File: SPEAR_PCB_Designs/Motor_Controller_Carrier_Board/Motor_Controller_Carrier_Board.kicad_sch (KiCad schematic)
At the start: 16 parts, among them J1 Conn_01x02_Pin, J2 Conn_01x02_Pin, J3 Conn_01x02_Pin, J4 JST_S4B-XH-A-1, U1 AP63203WU

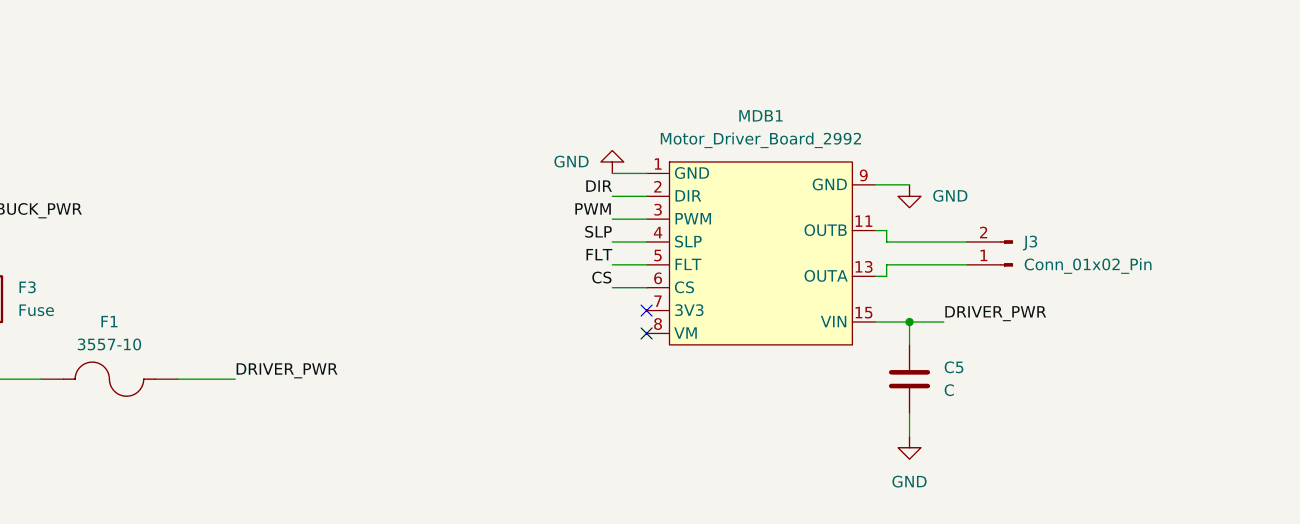
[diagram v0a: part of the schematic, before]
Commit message: Moved power traces to the front and made minor adjustments to the layout of the carrier board
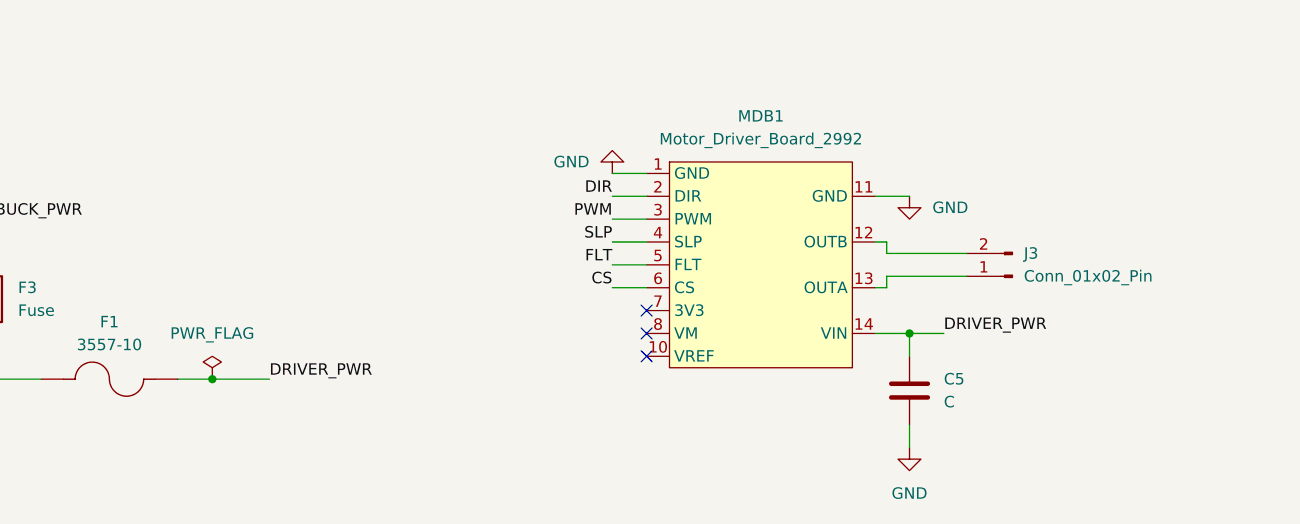
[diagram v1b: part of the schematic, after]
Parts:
- C1: DigiKey_Part_Number (none) -> 445-173297-1-ND
- C2, C4: DigiKey_Part_Number (none) -> 445-173319-1-ND
- C3: DigiKey_Part_Number (none) -> 56-K104K15X7RF53H5G-ND
- C5: DigiKey_Part_Number (none) -> 493-15942-ND
- F1: DigiKey_Part_Number (none) -> 36-3557-10-ND
- F2: DigiKey_Part_Number (none) -> 36-3557-15-ND
- F3: DigiKey_Part_Number (none) -> F5502CT-ND
- J4: DigiKey_Part_Number (none) -> 455-S4B-XH-A-1-ND
- L1: DigiKey_Part_Number (none) -> 732-74437368039CT-ND
- MCB1, MDB1: now left out of the parts list
- U1: DigiKey_Part_Number (none) -> AP63203WU-7DICT-ND
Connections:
- net DRIVER_PWR: now also MDB1.14 (VIN); no longer MDB1.15 (VIN), MDB1.16 (VIN)
- net GND: now also MDB1.11 (GND), MDB1.15 (GND), MDB1.16 (GND); no longer MDB1.10 (GND)
- net at J3.1 (Pin_1), MDB1.13 (OUTA): no longer MDB1.14 (OUTA)
- net at J3.2 (Pin_2), MDB1.12 (OUTB): no longer MDB1.11 (OUTB)
- no-connect marks 31 -> 32
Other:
- moved on the sheet: C5, J3

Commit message: Almost finished getting carrier board ready for fabrication
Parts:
- C3: footprint Capacitor_THT:C_Disc_D5.0mm_W2.5mm_P5.00mm -> Motor_Controller_Carrier_Board:C_Disc_D5.0mm_W2.5mm_P5.00mm
- J1, J2, J3: footprint Connector_AMASS:AMASS_XT30PW-M_1x02_P2.50mm_Horizontal -> SPEAR_Connectors:AMASS_XT30PW-M_1x02_P2.50mm_Horizontal_1; now left out of the parts list
- J4: footprint Connector_JST:JST_XH_S4B-XH-A-1_1x04_P2.50mm_Horizontal -> SPEAR_Connectors:JST_XH_S4B-XH-A-1_1x04_P2.50mm_Horizontal
- U1: footprint Package_TO_SOT_SMD:TSOT-23-6 -> Motor_Controller_Carrier_Board:TSOT-23-6
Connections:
- net DRIVER_PWR: now also MDB1.22 (VIN), MDB1.23 (VIN), MDB1.24 (VIN); no longer MDB1.14 (VIN)
- net GND: now also MDB1.12 (GND), MDB1.13 (GND), MDB1.14 (GND); no longer MDB1.16 (GND)
- net at J3.1 (Pin_1): now also MDB1.19 (OUTA), MDB1.20 (OUTA), MDB1.21 (OUTA); no longer MDB1.13 (OUTA)
- net at J3.2 (Pin_2): now also MDB1.16 (OUTB), MDB1.17 (OUTB), MDB1.18 (OUTB); no longer MDB1.12 (OUTB)
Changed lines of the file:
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@@
 		(unit 1)
 		(exclude_from_sim no)
-		(in_bom yes)
+		(in_bom no)
 		(on_board yes)
 		(dnp no)
@@
 			)
 		)
-		(property "Footprint" "Connector_AMASS:AMASS_XT30PW-M_1x02_P2.50mm_Horizontal"
+		(property "Footprint" "SPEAR_Connectors:AMASS_XT30PW-M_1x02_P2.50mm_Horizontal_1"
 			(at 213.36 130.81 0)
 			(effects
@@
 		(pin "16"
 		)
+		(pin "17"
+		)
+		(pin "19"
+		)
+		(pin "22"
+		)
+		(pin "24"
+		)
+		(pin "21"
+		)
+		(pin "18"
+		)
+		(pin "20"
+		)
+		(pin "23"
+		)
 		(instances
 			(project ""
@@
 			)
 		)
-		(property "Footprint" "Package_TO_SOT_SMD:TSOT-23-6"
+		(property "Footprint" "Motor_Controller_Carrier_Board:TSOT-23-6"
 			(at 64.77 96.52 0)
 			(effects
@@
 		(unit 1)
 		(exclude_from_sim no)
-		(in_bom yes)
+		(in_bom no)
 		(on_board yes)
 		(dnp no)
@@
 			)
 		)
-		(property "Footprint" "Connector_AMASS:AMASS_XT30PW-M_1x02_P2.50mm_Horizontal"
+		(property "Footprint" "SPEAR_Connectors:AMASS_XT30PW-M_1x02_P2.50mm_Horizontal_1"
 			(at 77.47 144.78 0)
 			(effects
@@
 			)
 		)
-		(property "Footprint" "Capacitor_THT:C_Disc_D5.0mm_W2.5mm_P5.00mm"
+		(property "Footprint" "Motor_Controller_Carrier_Board:C_Disc_D5.0mm_W2.5mm_P5.00mm"
 			(at 80.9752 73.66 0)
 			(effects
@@
 		(unit 1)
 		(exclude_from_sim no)
-		(in_bom yes)
+		(in_bom no)
 		(on_board yes)
 		(dnp no)
@@
 			)
 		)
-		(property "Footprint" "Connector_AMASS:AMASS_XT30PW-M_1x02_P2.50mm_Horizontal"
+		(property "Footprint" "SPEAR_Connectors:AMASS_XT30PW-M_1x02_P2.50mm_Horizontal_1"
 			(at 77.47 116.84 0)
 			(effects
@@
 			)
 		)
-		(property "Footprint" "Connector_JST:JST_XH_S4B-XH-A-1_1x04_P2.50mm_Horizontal"
+		(property "Footprint" "SPEAR_Connectors:JST_XH_S4B-XH-A-1_1x04_P2.50mm_Horizontal"
 			(at 238.76 74.93 0)
 			(effects

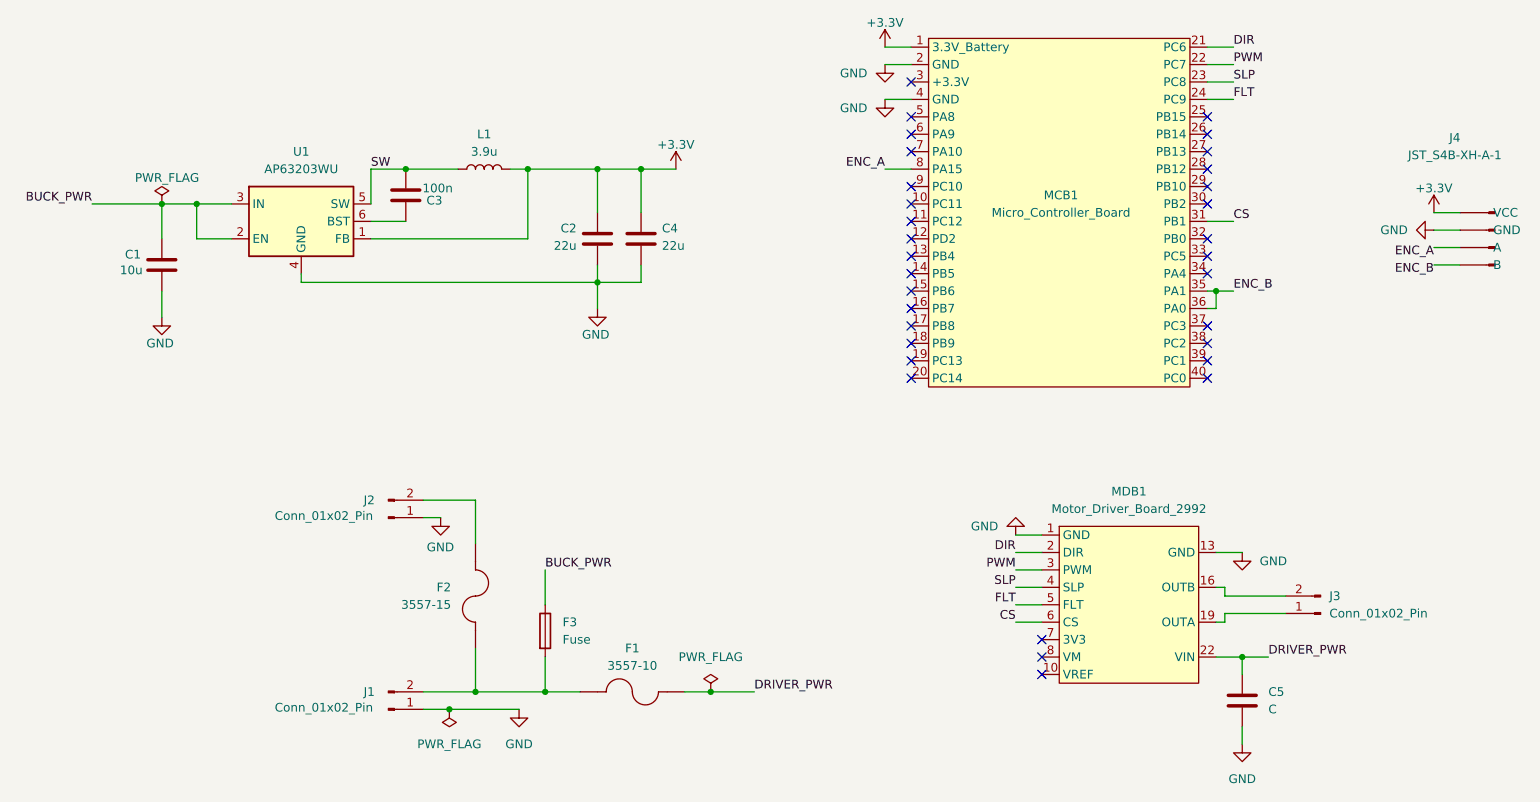
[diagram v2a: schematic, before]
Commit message: Added board-to-board connectors to schematic and swapped out THT capacitors for SMT ones in carrier board
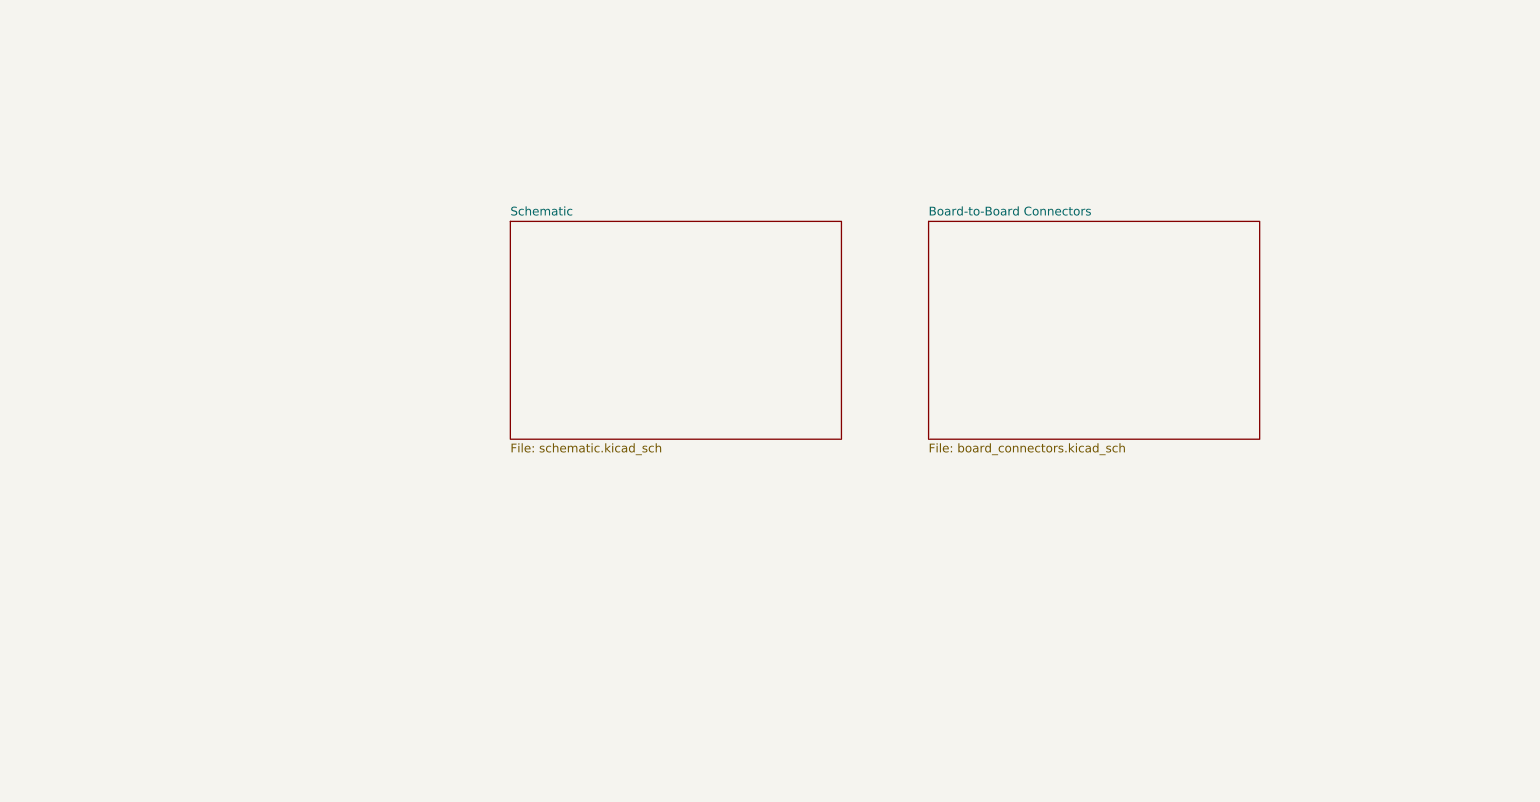
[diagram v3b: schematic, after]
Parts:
- removed C1: 10u, SPEAR_AP63203BuckConverter:CAP_FG20_TDK_C1, symbol Device:C
- removed C2, C4: 22u, SPEAR_AP63203BuckConverter:CAP_FG22_TDK_C2_C4, symbol Device:C
- removed C3: 100n, Motor_Controller_Carrier_Board:C_Disc_D5.0mm_W2.5mm_P5.00mm, symbol Device:C
- removed C5: C, Motor_Controller_Carrier_Board:CAP_UBY_18X20_NCH, symbol Device:C
- removed F1: 3557-10, Motor_Controller_Carrier_Board:FUSE_3557-10, symbol Motor_Controller_Carrier_Board:3557-10
- removed F2: 3557-15, Motor_Controller_Carrier_Board:FUSE_3557-15, symbol Motor_Controller_Carrier_Board:3557-10
- removed F3: Fuse, Motor_Controller_Carrier_Board:FUS_LITTELFUSE_392_LTF, symbol Device:Fuse
- removed J1, J2, J3: Conn_01x02_Pin, SPEAR_Connectors:AMASS_XT30PW-M_1x02_P2.50mm_Horizontal_1, symbol Connector:Conn_01x02_Pin
- removed J4: JST_S4B-XH-A-1, SPEAR_Connectors:JST_XH_S4B-XH-A-1_1x04_P2.50mm_Horizontal, symbol Motor_Controller_Carrier_Board:JST_S4B-XH-A-1
- removed L1: 3.9u, SPEAR_AP63203BuckConverter:L_Wurth_WE-LHMI-1040_L1, symbol Device:L
- removed MCB1: Micro_Controller_Board, SPEAR_Boards:Micro_Controller_Board, symbol SPEAR_Boards:Micro_Controller_Board
- removed MDB1: Motor_Driver_Board_2992, SPEAR_Boards:Motor_Driver_Board_2992, symbol SPEAR_Boards:Motor_Driver_Board_2992
- removed U1: AP63203WU, Motor_Controller_Carrier_Board:TSOT-23-6, symbol Regulator_Switching:AP63203WU
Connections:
- no-connect marks 32 -> 0
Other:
- added sheet Board-to-Board Connectors (board_connectors.kicad_sch)
- added sheet Schematic (schematic.kicad_sch)
